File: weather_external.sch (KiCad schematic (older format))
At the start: 19 parts, among them J1 Conn_01x06_Male, J2 Conn_01x02_Male, J3 Conn_01x03_Male, J4 Conn_01x04_Male, Q1 IRF510PBF, SW1 SW_Push, U1 MCP1700-3302E_SOT23, U3 NE555DR

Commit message: Version 1.2. Small components
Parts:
- removed C2: 220uF, Capacitor_THT:CP_Radial_D4.0mm_P2.00mm, symbol Device:CP
- removed C3, C5: 0.1uF, Capacitor_THT:CP_Radial_D4.0mm_P2.00mm, symbol Device:CP
- removed J1: Conn_01x06_Male, Connector_PinHeader_2.54mm:PinHeader_1x06_P2.54mm_Vertical, symbol Connector:Conn_01x06_Male
- removed Q1: IRF510PBF, digikey-footprints:TO-220-3, symbol dk_Transistors-FETs-MOSFETs-Single:IRF510PBF
- removed R1, R3, R4: 10k, Resistor_THT:R_Axial_DIN0207_L6.3mm_D2.5mm_P7.62mm_Horizontal, symbol Device:R
- added C1: 0.1uf, Capacitor_THT:CP_Radial_D4.0mm_P1.50mm, symbol Device:C
- added C2: 47uf, Capacitor_THT:CP_Radial_D4.0mm_P1.50mm, symbol Device:C
- added FTDI1: Conn_01x04_Male, Connector_PinHeader_2.54mm:PinHeader_1x04_P2.54mm_Vertical, symbol Connector:Conn_01x04_Male
- added J5: Conn_01x02_Male, Connector_PinHeader_2.54mm:PinHeader_1x02_P2.54mm_Vertical, symbol Connector:Conn_01x02_Male
- added L1: INDUCTOR, Inductor_SMD:L_0805_2012Metric_Pad1.15x1.40mm_HandSolder, symbol pspice:INDUCTOR
- added R2, R3, R4: 10k, Resistor_SMD:R_1206_3216Metric, symbol Device:R_Small
- added R5: 100k, Resistor_SMD:R_1206_3216Metric, symbol Device:R_Small
- added R6: 270k, Resistor_SMD:R_1206_3216Metric, symbol Device:R_Small
- J2: footprint Connector_PinHeader_2.54mm:PinHeader_1x02_P2.54mm_Vertical -> Connector_JST:JST_PH_B2B-PH-K_1x02_P2.00mm_Vertical
- U3: footprint Package_DIP:DIP-8_W7.62mm -> Package_SO:SOIC-8_3.9x4.9mm_P1.27mm
- renumbered J4 to I2C1, R5 to R1
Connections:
- net labels added: +3.3V
- wire segments 153 -> 129
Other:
- moved on the sheet: J2

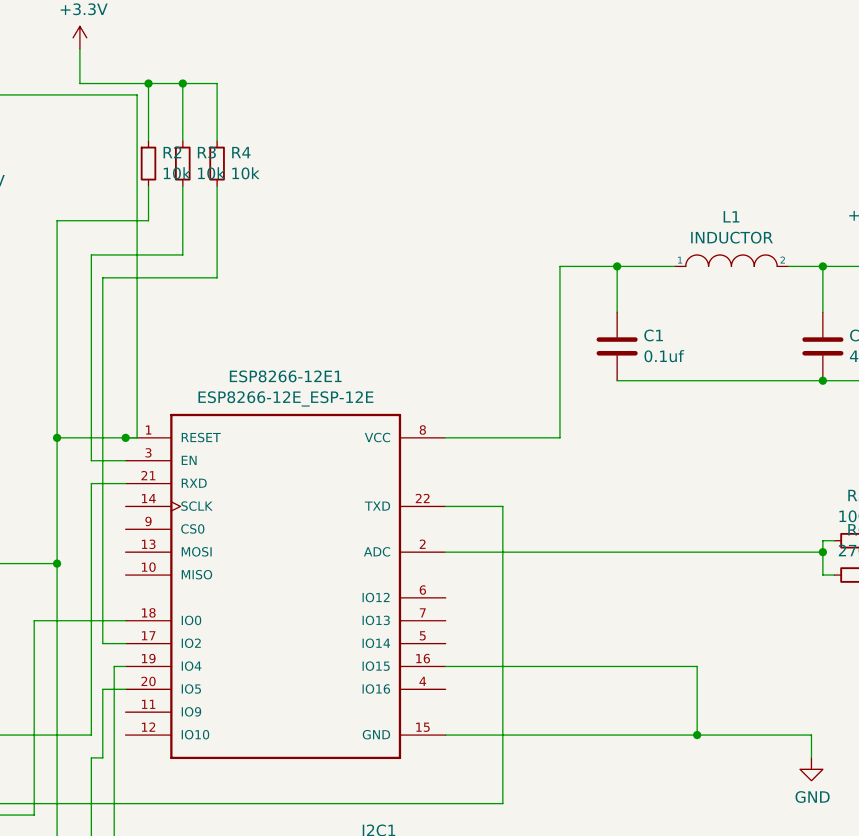
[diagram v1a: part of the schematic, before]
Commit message: Version with 555
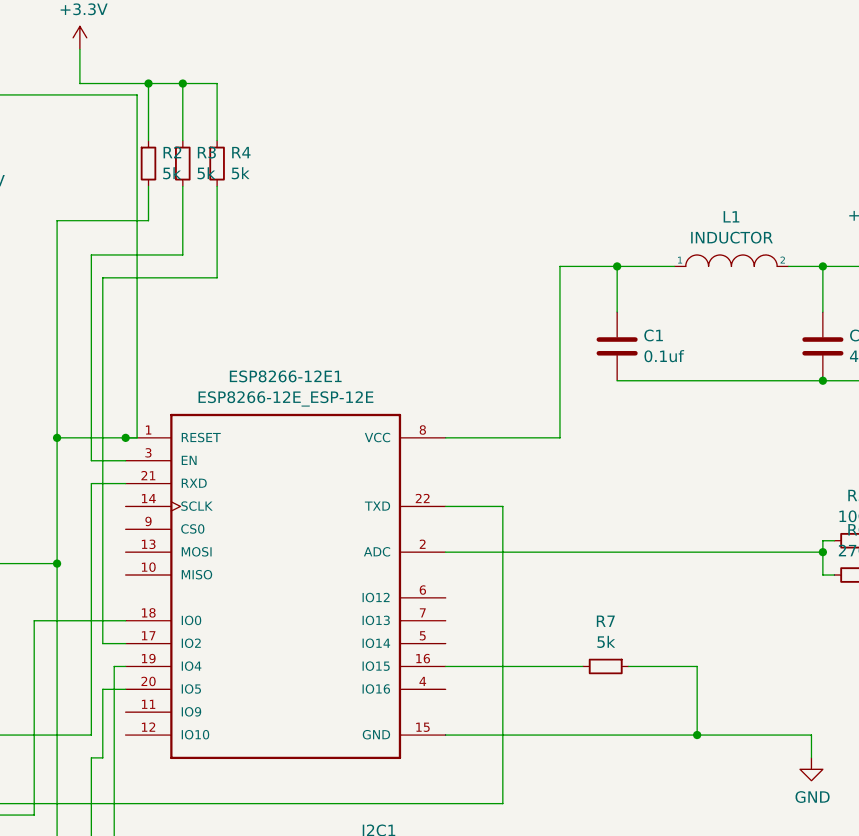
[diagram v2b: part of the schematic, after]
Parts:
- added R7: 5k, Resistor_SMD:R_1206_3216Metric, symbol Device:R_Small
- R2, R3, R4: value 10k -> 5k
- SW1: footprint Button_Switch_THT:SW_PUSH_6mm -> Button_Switch_SMD:SW_SPST_CK_RS282G05A3
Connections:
- net GND: now also R7.1; no longer ESP8266-12E1.16 (IO15)
- new net: ESP8266-12E1.16 (IO15), R7.2
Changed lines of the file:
@@
 F 0 "SW1" H 5150 3065 50  0000 C CNN
 F 1 "SW_Push" H 5150 3156 50  0000 C CNN
-F 2 "Button_Switch_THT:SW_PUSH_6mm" H 5150 3450 50  0001 C CNN
+F 2 "Button_Switch_SMD:SW_SPST_CK_RS282G05A3" H 5150 3450 50  0001 C CNN
 F 3 "~" H 5150 3450 50  0001 C CNN
 	1    5150 3250
@@
 	6000 3700 6050 3700
 Wire Wire Line
-	7450 3700 8550 3700
-Wire Wire Line
 	8550 3700 8550 4000
 Wire Wire Line
@@
 $EndComp
 Wire Wire Line
-	8550 4000 9050 4000
-Wire Wire Line
 	9050 4000 9050 4100
-Connection ~ 8550 4000
 $Comp
 L power:GND #PWR0111
@@
 P 6150 1500
 F 0 "R2" H 6209 1546 50  0000 L CNN
-F 1 "10k" H 6209 1455 50  0000 L CNN
+F 1 "5k" H 6209 1455 50  0000 L CNN
 F 2 "Resistor_SMD:R_1206_3216Metric" H 6150 1500 50  0001 C CNN
 F 3 "~" H 6150 1500 50  0001 C CNN
@@
 P 6300 1500
 F 0 "R3" H 6359 1546 50  0000 L CNN
-F 1 "10k" H 6359 1455 50  0000 L CNN
+F 1 "5k" H 6359 1455 50  0000 L CNN
 F 2 "Resistor_SMD:R_1206_3216Metric" H 6300 1500 50  0001 C CNN
 F 3 "~" H 6300 1500 50  0001 C CNN
@@
 P 6450 1500
 F 0 "R4" H 6509 1546 50  0000 L CNN
-F 1 "10k" H 6509 1455 50  0000 L CNN
+F 1 "5k" H 6509 1455 50  0000 L CNN
 F 2 "Resistor_SMD:R_1206_3216Metric" H 6450 1500 50  0001 C CNN
 F 3 "~" H 6450 1500 50  0001 C CNN
@@
 Wire Wire Line
 	4750 2950 4750 3250
+$Comp
+L Device:R_Small R7
+U 1 1 5FC4EDAF
+P 8150 3700
+F 0 "R7" V 7954 3700 50  0000 C CNN
+F 1 "5k" V 8045 3700 50  0000 C CNN
+F 2 "Resistor_SMD:R_1206_3216Metric" H 8150 3700 50  0001 C CNN
+F 3 "~" H 8150 3700 50  0001 C CNN
+	1    8150 3700
+	0    1    1    0
+$EndComp
+Connection ~ 8550 4000
+Wire Wire Line
+	8550 4000 9050 4000
+Wire Wire Line
+	7450 3700 8050 3700
+Wire Wire Line
+	8250 3700 8550 3700
 $EndSCHEMATC

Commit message: SMD Components
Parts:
- removed C4: 220uf, Capacitor_THT:CP_Radial_D4.0mm_P2.00mm, symbol Device:CP
- removed J3: Conn_01x03_Male, Connector_PinHeader_2.54mm:PinHeader_1x03_P2.54mm_Vertical, symbol Connector:Conn_01x03_Male
- removed J5: Conn_01x02_Male, Connector_PinHeader_2.54mm:PinHeader_1x02_P2.54mm_Vertical, symbol Connector:Conn_01x02_Male
- removed JP1: Jumper_2_Open, Connector_PinHeader_2.54mm:PinHeader_1x02_P2.54mm_Vertical, symbol Jumper:Jumper_2_Open
- removed R1: 220, Resistor_THT:R_Axial_DIN0207_L6.3mm_D2.5mm_P7.62mm_Horizontal, symbol Device:R
- removed RV1: 1M, Potentiometer_THT:Potentiometer_Vishay_T73YP_Vertical, symbol Device:R_POT
- removed U1: MCP1700-3302E_SOT23, Package_TO_SOT_SMD:SOT-23, symbol Regulator_Linear:MCP1700-3302E_SOT23
- removed U3: NE555DR, Package_SO:SOIC-8_3.9x4.9mm_P1.27mm, symbol dk_Clock-Timing-Programmable-Timers-and-Oscillators:NE555DR
- added JP1: Jumper_NO_Small, Connector_PinHeader_2.54mm:PinHeader_1x02_P2.54mm_Vertical, symbol Device:Jumper_NO_Small
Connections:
- net VCC is gone; now on net +3V3: J2.1 (Pin_1), R5.1
- net at ESP8266-12E1.1 (RESET), FTDI1.3 (Pin_3), R2.2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: now also JP1.1
- net at ESP8266-12E1.4 (IO16): now also JP1.2

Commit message: no 555 Print version
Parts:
- removed L1: INDUCTOR, Inductor_SMD:L_0805_2012Metric_Pad1.15x1.40mm_HandSolder, symbol pspice:INDUCTOR
- removed R7: 5k, Resistor_SMD:R_1206_3216Metric, symbol Device:R_Small
- added J1: Conn_01x02_Male, Connector_PinHeader_2.54mm:PinHeader_1x02_P2.54mm_Vertical, symbol Connector:Conn_01x02_Male
- added R1: 5k, Resistor_THT:R_Axial_DIN0207_L6.3mm_D2.5mm_P7.62mm_Horizontal, symbol Device:R_Small
- R2, R3, R4, R5, R6: footprint Resistor_SMD:R_1206_3216Metric -> Resistor_THT:R_Axial_DIN0207_L6.3mm_D2.5mm_P7.62mm_Horizontal
- SW1: footprint Button_Switch_SMD:SW_SPST_CK_RS282G05A3 -> Button_Switch_THT:SW_PUSH_6mm
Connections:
- net +3V3: now also C1.1, ESP8266-12E1.8 (VCC), J1.1 (Pin_1), R1.1
- net GND: now also ESP8266-12E1.16 (IO15), J1.2 (Pin_2)
- net at FTDI1.1 (Pin_1): now also ESP8266-12E1.18 (IO0), R1.2; no longer ESP8266-12E1.21 (RXD)
- net at ESP8266-12E1.1 (RESET), JP1.1, R2.2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: now also FTDI1.4 (Pin_4); no longer FTDI1.3 (Pin_3)
- new net: ESP8266-12E1.21 (RXD), FTDI1.3 (Pin_3)
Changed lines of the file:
@@
 F 0 "SW1" H 5150 3065 50  0000 C CNN
 F 1 "SW_Push" H 5150 3156 50  0000 C CNN
-F 2 "Button_Switch_SMD:SW_SPST_CK_RS282G05A3" H 5150 3450 50  0001 C CNN
+F 2 "Button_Switch_THT:SW_PUSH_6mm" H 5150 3450 50  0001 C CNN
 F 3 "~" H 5150 3450 50  0001 C CNN
 	1    5150 3250
@@
 	6050 3500 5650 3500
 Wire Wire Line
-	5650 3500 5650 4350
+	5650 3500 5650 3900
 Wire Wire Line
 	6050 3600 5950 3600
@@
 $EndComp
 Wire Wire Line
-	3650 4200 3800 4200
-Wire Wire Line
-	3800 4200 3800 4550
-Wire Wire Line
-	3650 4300 3650 4350
-Wire Wire Line
-	3650 4000 5900 4000
-Wire Wire Line
-	3650 4350 5650 4350
-Wire Wire Line
 	3650 4100 4400 4100
 Wire Wire Line
@@
 F 3 "" H 4750 3650 50  0001 C CNN
 	1    4750 3650
-	1    0    0    -1
-$EndComp
-$Comp
-L pspice:INDUCTOR L1
-U 1 1 5FB2D88D
-P 8700 1950
-F 0 "L1" H 8700 2165 50  0000 C CNN
-F 1 "INDUCTOR" H 8700 2074 50  0000 C CNN
-F 2 "Inductor_SMD:L_0805_2012Metric_Pad1.15x1.40mm_HandSolder" H 8700 1950 50  0001 C CNN
-F 3 "~" H 8700 1950 50  0001 C CNN
-	1    8700 1950
 	1    0    0    -1
 $EndComp
@@
 	8200 2150 8200 1950
 Wire Wire Line
-	8200 1950 8450 1950
-Wire Wire Line
-	8950 1950 9100 1950
-Wire Wire Line
 	9100 1950 9100 2150
 Wire Wire Line
@@
 	5850 1150 5850 1000
 Wire Wire Line
-	6150 1150 5850 1150
+	6150 1150 6000 1150
 Connection ~ 6150 1150
 Wire Wire Line
@@
 F 0 "R2" H 6209 1546 50  0000 L CNN
 F 1 "5k" H 6209 1455 50  0000 L CNN
-F 2 "Resistor_SMD:R_1206_3216Metric" H 6150 1500 50  0001 C CNN
+F 2 "Resistor_THT:R_Axial_DIN0207_L6.3mm_D2.5mm_P7.62mm_Horizontal" H 6150 1500 50  0001 C CNN
 F 3 "~" H 6150 1500 50  0001 C CNN
 	1    6150 1500
@@
 F 0 "R3" H 6359 1546 50  0000 L CNN
 F 1 "5k" H 6359 1455 50  0000 L CNN
-F 2 "Resistor_SMD:R_1206_3216Metric" H 6300 1500 50  0001 C CNN
+F 2 "Resistor_THT:R_Axial_DIN0207_L6.3mm_D2.5mm_P7.62mm_Horizontal" H 6300 1500 50  0001 C CNN
 F 3 "~" H 6300 1500 50  0001 C CNN
 	1    6300 1500
@@
 F 0 "R4" H 6509 1546 50  0000 L CNN
 F 1 "5k" H 6509 1455 50  0000 L CNN
-F 2 "Resistor_SMD:R_1206_3216Metric" H 6450 1500 50  0001 C CNN
+F 2 "Resistor_THT:R_Axial_DIN0207_L6.3mm_D2.5mm_P7.62mm_Horizontal" H 6450 1500 50  0001 C CNN
 F 3 "~" H 6450 1500 50  0001 C CNN
 	1    6450 1500
@@
 F 0 "R5" V 9054 3150 50  0000 C CNN
 F 1 "100k" V 9145 3150 50  0000 C CNN
-F 2 "Resistor_SMD:R_1206_3216Metric" H 9250 3150 50  0001 C CNN
+F 2 "Resistor_THT:R_Axial_DIN0207_L6.3mm_D2.5mm_P7.62mm_Horizontal" H 9250 3150 50  0001 C CNN
 F 3 "~" H 9250 3150 50  0001 C CNN
 	1    9250 3150
@@
 F 0 "R6" V 9054 3300 50  0000 C CNN
 F 1 "270k" V 9145 3300 50  0000 C CNN
-F 2 "Resistor_SMD:R_1206_3216Metric" H 9250 3300 50  0001 C CNN
+F 2 "Resistor_THT:R_Axial_DIN0207_L6.3mm_D2.5mm_P7.62mm_Horizontal" H 9250 3300 50  0001 C CNN
 F 3 "~" H 9250 3300 50  0001 C CNN
 	1    9250 3300
@@
 Wire Wire Line
 	9100 3200 9100 3300
-$Comp
-L Device:R_Small R7
-U 1 1 5FC4EDAF
-P 8150 3700
-F 0 "R7" V 7954 3700 50  0000 C CNN
-F 1 "5k" V 8045 3700 50  0000 C CNN
-F 2 "Resistor_SMD:R_1206_3216Metric" H 8150 3700 50  0001 C CNN
-F 3 "~" H 8150 3700 50  0001 C CNN
-	1    8150 3700
-	0    1    1    0
-$EndComp
 Connection ~ 8550 4000
 Wire Wire Line
 	8550 4000 9050 4000
-Wire Wire Line
-	7450 3700 8050 3700
-Wire Wire Line
-	8250 3700 8550 3700
 $Comp
 L Device:Jumper_NO_Small JP1
@@
 	6000 2700 5750 2700
 $Comp
-L power:+3.3V #PWR?
+L power:+3.3V #PWR0101
 U 1 1 5FEA3AAB
 P 9700 3150
-F 0 "#PWR?" H 9700 3000 50  0001 C CNN
+F 0 "#PWR0101" H 9700 3000 50  0001 C CNN
 F 1 "+3.3V" H 9715 3323 50  0000 C CNN
 F 2 "" H 9700 3150 50  0001 C CNN
@@
 	1    0    0    -1
 $EndComp
+Wire Wire Line
+	8200 1950 9100 1950
+Wire Wire Line
+	3800 4550 3800 4300
+Wire Wire Line
+	3800 4300 3650 4300
+Wire Wire Line
+	5900 4000 4900 4000
+Wire Wire Line
+	4900 4000 4900 4200
+Wire Wire Line
+	4900 4200 3650 4200
+Wire Wire Line
+	5650 3900 3650 3900
+Wire Wire Line
+	3650 3900 3650 4000
+$Comp
+L Device:R_Small R1
+U 1 1 5F949756
+P 6000 1500
+F 0 "R1" H 6059 1546 50  0000 L CNN
+F 1 "5k" H 6059 1455 50  0000 L CNN
+F 2 "Resistor_THT:R_Axial_DIN0207_L6.3mm_D2.5mm_P7.62mm_Horizontal" H 6000 1500 50  0001 C CNN
+F 3 "~" H 6000 1500 50  0001 C CNN
+	1    6000 1500
+	1    0    0    -1
+$EndComp
+Wire Wire Line
+	6000 1600 5650 1600
+Wire Wire Line
+	5650 1600 5650 3500
+Connection ~ 5650 3500
+Wire Wire Line
+	6000 1400 6000 1150
+Connection ~ 6000 1150
+Wire Wire Line
+	6000 1150 5850 1150
+$Comp
+L Connector:Conn_01x02_Male J1
+U 1 1 5F94EE4D
+P 3450 4700
+F 0 "J1" H 3558 4881 50  0000 C CNN
+F 1 "Conn_01x02_Male" H 3558 4790 50  0000 C CNN
+F 2 "Connector_PinHeader_2.54mm:PinHeader_1x02_P2.54mm_Vertical" H 3450 4700 50  0001 C CNN
+F 3 "~" H 3450 4700 50  0001 C CNN
+	1    3450 4700
+	1    0    0    -1
+$EndComp
+$Comp
+L power:+3.3V #PWR0103
+U 1 1 5F94FAC5
+P 3050 4650
+F 0 "#PWR0103" H 3050 4500 50  0001 C CNN
+F 1 "+3.3V" H 3065 4823 50  0000 C CNN
+F 2 "" H 3050 4650 50  0001 C CNN
+F 3 "" H 3050 4650 50  0001 C CNN
+	1    3050 4650
+	1    0    0    -1
+$EndComp
+Wire Wire Line
+	3650 4700 3050 4700
+Wire Wire Line
+	3050 4700 3050 4650
+$Comp
+L power:GND #PWR0104
+U 1 1 5F952B0E
+P 3050 4800
+F 0 "#PWR0104" H 3050 4550 50  0001 C CNN
+F 1 "GND" H 3055 4627 50  0000 C CNN
+F 2 "" H 3050 4800 50  0001 C CNN
+F 3 "" H 3050 4800 50  0001 C CNN
+	1    3050 4800
+	1    0    0    -1
+$EndComp
+Wire Wire Line
+	3650 4800 3050 4800
+Wire Wire Line
+	7450 3700 8550 3700
 $EndSCHEMATC
